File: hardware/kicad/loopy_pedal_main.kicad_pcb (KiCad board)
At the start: 2 copper layers, 82 x 94 mm, 89 parts, among them J1 USB, J10 MOCO, J11 IND, J12 UNDO, J13 MODE, J14 TRACK1, J15 TRACK2, J16 TRACK3, J17 TRACK4, J18 CLEAR, J19 BANK, J2 9V, J3 RECPLAY, J4 STOP, J5 RING, J6 ICSP U1, J7 ICSP U2, J8 MIDI OUT, J9 MIDI IN, Q1 AO3401A, SW1 RST U1, SW2 RST U2, U1 ATmega328P-A, U10 74AHCT1G08, U2 ATmega16U2-A, U3 AP63203WU, U4 74AHCT1G125, U5 LM66100DCK, U6 LM66100DCK, U7 USBLC6-2SC6, U8 74AHCT1G125, U9 H11L1, Y1 16MHz, Y2 16MHz

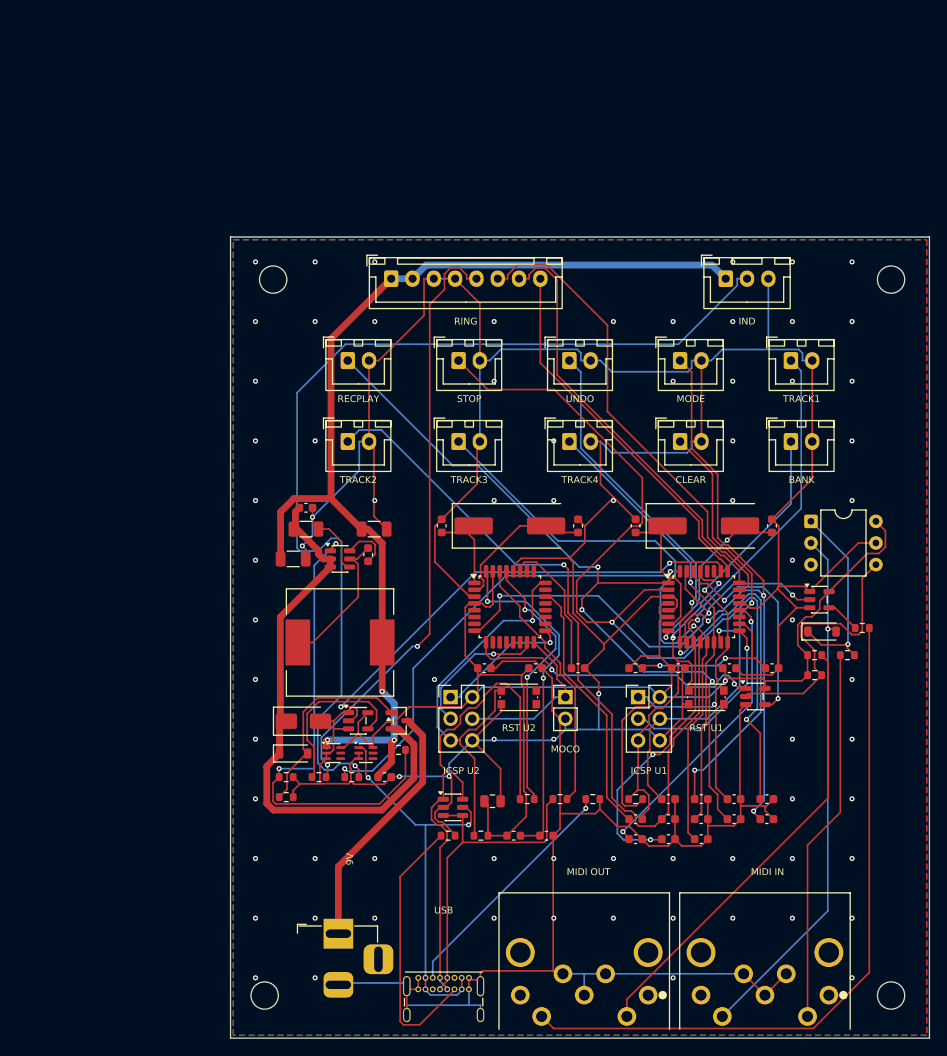
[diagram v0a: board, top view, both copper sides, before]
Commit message: feat(hardware): THT Loopy pedal main + ring boards, fab-ready
Through-hole MIDI looper foot-pedal: two KiCad 10 boards generated from
SKiDL + a scripted place/route pipeline, ready for JLCPCB bare-board fab.

Main board (94x96mm):
- Arduino Pro Micro (ATmega32U4) native USB-MIDI, buffered DIN MIDI OUT
  (74AHCT125), opto-isolated DIN MIDI IN (H11L1)
- 9V centre-negative barrel -> reverse-protection Schottky + TVS -> buck
  (+5V_LED for the LED ring); Pro Micro powered via RAW (onboard reg -> VCC)
- 10 footswitch headers, faceplate RESET (J20) + 6-pin ICSP (J21) recovery
- Fully silk-labelled (functions + component values), 4x M3 GND-bonded holes

Ring board (60mm round):
- Hosts an off-the-shelf 16-LED WS2812 NeoPixel module + EC11 encoder,
  8-pin link to the main board; 4-pad module mount (DIN/+5V/GND + DOUT post)

Both boards DRC-clean; gerbers + BOM/CPL in fab/. Vendored footprints and
3D models in loopy.pretty/. Plan-of-record in loopy_pedal_pcb_tht_plan.md.
Firmware skeleton (USB-MIDI + Serial1 DIN + footswitch debounce) in firmware/.
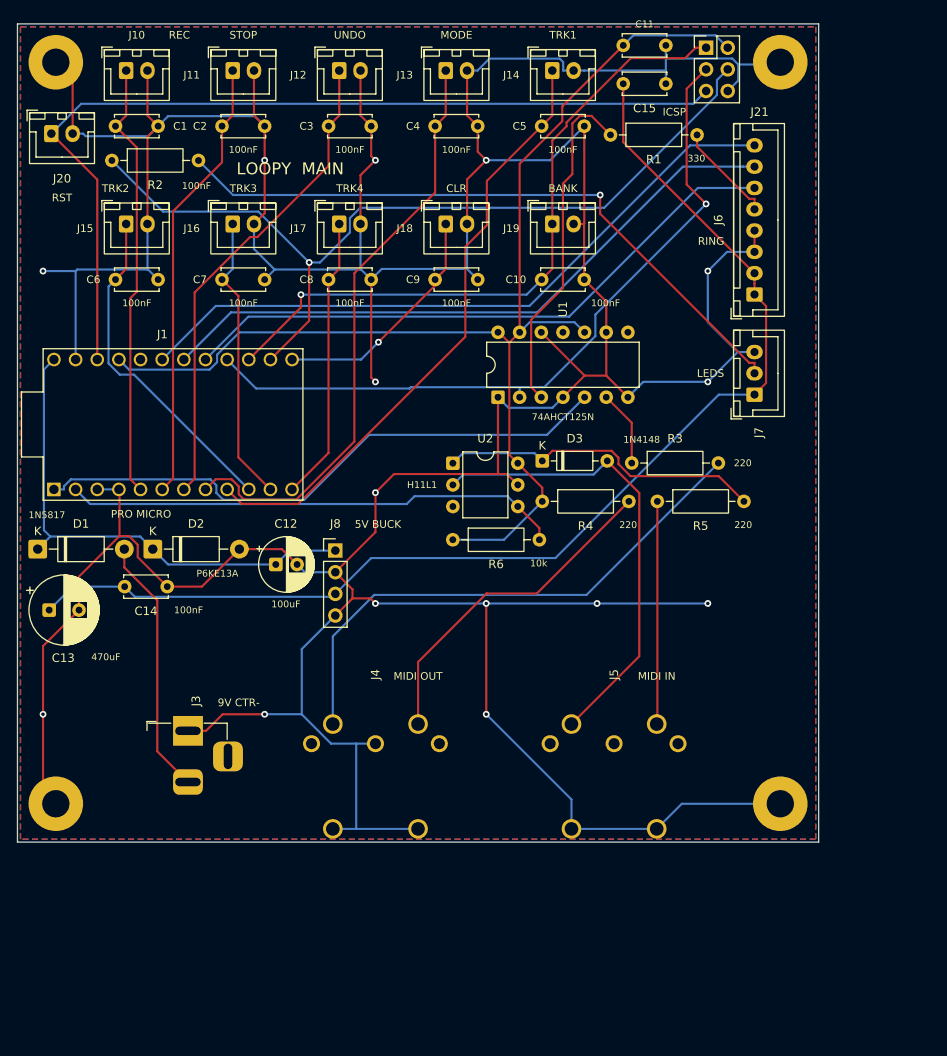
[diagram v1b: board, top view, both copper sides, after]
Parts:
- removed C16, C19, C20, C25, C28, C29, C30: 100nF, C_0603_1608Metric
- removed C17, C18: 1nF, C_0603_1608Metric
- removed C21: 1uF, C_0603_1608Metric
- removed C22, C23: 22pF, C_0603_1608Metric
- removed C24, C26, C27: 22uF, C_1206_3216Metric
- removed FB1, FB2: FerriteBead, L_0603_1608Metric
- removed J2: 9V, BarrelJack_Horizontal
- removed J9: MIDI IN, MIDI_DIN5_RA
- removed L1: 10uH, L_12x12mm_H8mm
- removed Q1: AO3401A, SOT-23
- removed R10, R11, R12: 220, R_0603_1608Metric
- removed R13, R8: 10k, R_0603_1608Metric
- removed R14, R9: 330, R_0603_1608Metric
- removed R15: 100k, R_0603_1608Metric
- removed R7: 52.3k, R_0603_1608Metric
- removed SW1: RST U1, SW_Push_1P1T_NO_CK_KMR2
- removed SW2: RST U2, SW_Push_1P1T_NO_CK_KMR2
- removed U10: 74AHCT1G08, SOT-23-5
- removed U3: AP63203WU, SOT-23-6
- removed U4, U8: 74AHCT1G125, SOT-23-5
- removed U5, U6: LM66100DCK, SOT-363_SC-70-6
- removed U7: USBLC6-2SC6, SOT-23-6
- removed U9: H11L1, DIP-6_W7.62mm
- removed Y1, Y2: 16MHz, Crystal_SMD_HC49-SD
- added J20: RESET, JST_XH_B2B-XH-A_1x02_P2.50mm_Vertical, F.Cu at (8.97, 17.9)
- added J21: ICSP, PinHeader_2x03_P2.54mm_Vertical, F.Cu at (85.8, 7.79)
- C1, C10, C11, C14, C15, C2, C5, C6, C8, C9: footprint C_0603_1608Metric -> C_Disc_D5.0mm_W2.5mm_P5.00mm
- C12: value 100nF -> 100uF; footprint C_0603_1608Metric -> CP_Radial_D6.3mm_P2.50mm
- C13: value 100nF -> 470uF; footprint C_0603_1608Metric -> CP_Radial_D8.0mm_P3.50mm
- C3, C4: value 22pF -> 100nF; footprint C_0603_1608Metric -> C_Disc_D5.0mm_W2.5mm_P5.00mm
- C7: value 10uF -> 100nF; footprint C_0805_2012Metric -> C_Disc_D5.0mm_W2.5mm_P5.00mm
- D1: value SMAJ12A -> 1N5817; footprint D_SMA -> D_DO-41_SOD81_P10.16mm_Horizontal
- D2: value 1N4148 -> P6KE13A; footprint D_SOD-123 -> D_DO-41_SOD81_P10.16mm_Horizontal
- D3: value 10V -> 1N4148; footprint D_SOD-123 -> D_DO-35_SOD27_P7.62mm_Horizontal
- H1, H2, H3, H4: value MountingHole_3.2mm_M3 -> MountingHole_3.2mm_M3_Pad; footprint MountingHole_3.2mm_M3 -> MountingHole_3.2mm_M3_Pad
- J1: value USB -> ProMicro; footprint USB_C_Receptacle_GCT_USB4085 -> ProMicro
- J10: value MOCO -> FSW_RECPLAY; footprint PinHeader_1x02_P2.54mm_Vertical -> JST_XH_B2B-XH-A_1x02_P2.50mm_Vertical
- J11: value IND -> FSW_STOP; footprint JST_XH_B3B-XH-A_1x03_P2.50mm_Vertical -> JST_XH_B2B-XH-A_1x02_P2.50mm_Vertical
- J12: value UNDO -> FSW_UNDO
- J13: value MODE -> FSW_MODE
- J14: value TRACK1 -> FSW_TRACK1
- J15: value TRACK2 -> FSW_TRACK2
- J16: value TRACK3 -> FSW_TRACK3
- J17: value TRACK4 -> FSW_TRACK4
- J18: value CLEAR -> FSW_CLEAR
- J19: value BANK -> FSW_BANK
- J3: value RECPLAY -> Barrel_Jack; footprint JST_XH_B2B-XH-A_1x02_P2.50mm_Vertical -> BarrelJack_Horizontal
- J4: value STOP -> MIDI_DIN5_RA; footprint JST_XH_B2B-XH-A_1x02_P2.50mm_Vertical -> MIDI_DIN5_RA
- J5: value RING -> MIDI_DIN5_RA; footprint JST_XH_B8B-XH-A_1x08_P2.50mm_Vertical -> MIDI_DIN5_RA
- J6: value ICSP U1 -> Conn_01x08; footprint PinHeader_2x03_P2.54mm_Vertical -> JST_XH_B8B-XH-A_1x08_P2.50mm_Vertical
- J7: value ICSP U2 -> Conn_01x03; footprint PinHeader_2x03_P2.54mm_Vertical -> JST_XH_B3B-XH-A_1x03_P2.50mm_Vertical
- J8: value MIDI OUT -> BUCK_5V; footprint MIDI_DIN5_RA -> PinHeader_1x04_P2.54mm_Vertical
- R1: value 10k -> 330; footprint R_0603_1608Metric -> R_Axial_DIN0207_L6.3mm_D2.5mm_P10.16mm_Horizontal
- R2: value 22 -> 330; footprint R_0603_1608Metric -> R_Axial_DIN0207_L6.3mm_D2.5mm_P10.16mm_Horizontal
- R3: value 22 -> 220; footprint R_0603_1608Metric -> R_Axial_DIN0207_L6.3mm_D2.5mm_P10.16mm_Horizontal
- R4: value 10k -> 220; footprint R_0603_1608Metric -> R_Axial_DIN0207_L6.3mm_D2.5mm_P10.16mm_Horizontal
- R5: value 5.1k -> 220; footprint R_0603_1608Metric -> R_Axial_DIN0207_L6.3mm_D2.5mm_P10.16mm_Horizontal
- R6: value 5.1k -> 10k; footprint R_0603_1608Metric -> R_Axial_DIN0207_L6.3mm_D2.5mm_P10.16mm_Horizontal
- U1: value ATmega328P-A -> 74AHCT125N; footprint TQFP-32_7x7mm_P0.8mm -> DIP-14_W7.62mm
- U2: value ATmega16U2-A -> H11L1; footprint TQFP-32_7x7mm_P0.8mm -> DIP-6_W7.62mm
- moved C1 99.9 mm to (16.5, 17.0)
- moved C2 96.7 mm to (29.0, 17.0)
- moved J10 89.8 mm to (17.8, 10.5)
- moved R2 89.4 mm to (16.1, 21.0)
- moved C15 89.1 mm to (76.1, 12.0)
- moved C11 88.9 mm to (76.1, 7.53)
- moved C6 85.2 mm to (16.5, 35.0)
- moved D2 79.1 mm to (20.9, 66.6)
- moved R1 78.0 mm to (74.6, 18.0)
- moved C13 77.5 mm to (8.72, 73.8)
- moved C8 72.8 mm to (41.5, 35.0)
- moved C9 72.4 mm to (54.0, 35.0)
- moved J1 71.0 mm to (23.2, 52.0)
- moved C14 69.4 mm to (17.6, 71.0)
- moved C7 68.9 mm to (29.0, 35.0)
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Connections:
- C1 pad 1: N$1 -> SW_RECPLAY
- C10 pad 1: SW_STOP -> SW_BANK
- C11 pad 1: SW_UNDO -> +5V
- C12 pad 1: SW_MODE -> +9V
- C13 pad 1: SW_TRACK1 -> +5V_LED
- C14 pad 1: SW_TRACK2 -> +5V_LED
- C15 pad 1: SW_TRACK3 -> +5V_LED
- C2 pad 1: N$2 -> SW_STOP
- C3 pad 1: N$3 -> SW_UNDO
- C4 pad 1: N$4 -> SW_MODE
- C5 pad 1: +5V -> SW_TRACK1
- C6 pad 1: +5V -> SW_TRACK2
- C7 pad 1: +5V -> SW_TRACK3
- C8 pad 1: DTR -> SW_TRACK4
- C8 pad 2: RST_328 -> GND
- C9 pad 1: SW_RECPLAY -> SW_CLEAR
- D1 pad 2: GND -> VIN_RAW
- D2 pad 1: N$20 -> +9V
- D2 pad 2: N$21 -> GND
- D3 pad 1: +9V -> N$4
- D3 pad 2: Q1_GATE -> N$5
- J10 pad 1: N$11 -> SW_RECPLAY
- J11 pad 1: +5V_LED -> SW_STOP
- J11 pad 2: IND_DATA_OUT -> GND
- J3 pad 1: SW_RECPLAY -> GND
- J3 pad 2: GND -> VIN_RAW
- J4 pad 1: SW_STOP -> (no net)
- J5 pad 1: +5V_LED -> (no net)
- J5 pad 2: +5V_LED -> (no net)
- J5 pad 3: GND -> (no net)
- J5 pad 4: GND -> N$3
- J5 pad 5: RING_DATA_OUT -> N$5
- J5 pad 6: ENC_A -> GND
- J5 pad 7: ENC_B -> GND
- J6 pad 1: SW_BANK -> +5V_LED
- J6 pad 2: +5V -> +5V_LED
- J6 pad 3: N$5 -> GND
- J6 pad 4: SW_CLEAR -> GND
- J6 pad 5: RST_328 -> RING_DATA_OUT
- J6 pad 6: GND -> ENC_A
- J7 pad 1: N$12 -> +5V_LED
- J7 pad 2: +5V -> IND_DATA_OUT
- J7 pad 3: N$13 -> GND
- J8 pad 1: (no net) -> +9V
- J8 pad 3: (no net) -> +5V_LED
- J8 pad 4: N$18 -> GND
- R1 pad 1: RST_328 -> RING_DATA_BUF
- R1 pad 2: +5V -> RING_DATA_OUT
- R2 pad 1: USB_D+ -> IND_DATA
- R2 pad 2: N$9 -> IND_DATA_OUT
- R3 pad 1: USB_D- -> MIDI_OUT_BUF
- R3 pad 2: N$10 -> N$1
- R4 pad 1: RST_16 -> +5V
- R4 pad 2: +5V -> N$2
- R5 pad 1: N$14 -> N$3
- R5 pad 2: GND -> N$4
- R6 pad 1: N$15 -> +5V
- R6 pad 2: GND -> UART_RX
- U1 pad 1: SW_RECPLAY -> GND
- U1 pad 10: SW_MODE -> +5V
- U1 pad 11: SW_TRACK1 -> (no net)
- U1 pad 12: SW_TRACK2 -> GND
- U1 pad 13: SW_TRACK3 -> +5V
- U1 pad 14: SW_TRACK4 -> +5V
- U1 pad 2: SW_STOP -> RING_DATA
- U1 pad 3: GND -> RING_DATA_BUF
- U1 pad 4: +5V -> GND
- U1 pad 5: GND -> UART_TX
- U1 pad 6: +5V -> MIDI_OUT_BUF
- U1 pad 7: N$3 -> GND
- U1 pad 8: N$4 -> (no net)
- U1 pad 9: SW_UNDO -> GND
- U2 pad 1: N$7 -> N$4
- U2 pad 2: N$8 -> N$5
- U2 pad 3: GND -> (no net)
- U2 pad 4: +5V -> UART_RX
- U2 pad 5: (no net) -> GND
- U2 pad 6: (no net) -> +5V
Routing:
- net RST: track 0.00 -> 107.6 mm
- net N$17: track 82.2 -> 0.00 mm
- net N$21: track 62.6 -> 0.00 mm, vias 1 -> 0
- net USB_D+: track 62.4 -> 0.00 mm
- net RING_DATA_OUT: track 70.6 -> 11.9 mm, vias 2 -> 0
- net FB: track 57.0 -> 0.00 mm, vias 2 -> 0
- net SW_STOP: track 105.8 -> 52.6 mm, vias 2 -> 0
- net SW_TRACK2: track 92.9 -> 39.8 mm, vias 1 -> 0
- net N$18: track 52.5 -> 0.00 mm
- net RST_16: track 48.5 -> 0.00 mm, vias 1 -> 0
- net IND_DATA: track 54.4 -> 101.9 mm, vias 2 -> 1
- net VBUS: track 46.7 -> 0.00 mm, vias 2 -> 0
- net N$19: track 44.0 -> 0.00 mm
- net RST_328: track 43.6 -> 0.00 mm, vias 2 -> 0
- net N$1: track 20.4 -> 64.0 mm, vias 2 -> 0
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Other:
- board size 82 x 94 mm -> 94 x 96 mm
- board text added: "100nF"
- board text added: "100uF"
- board text added: "10k"
- board text added: "1N4148"
- board text added: "1N5817"
- board text added: "220"
- board text added: "330"
- board text added: "470uF"
- board text added: "5V BUCK"
- board text added: "74AHCT125N"
- board text added: "9V CTR-"
- board text added: "BANK"
- board text added: "CLR"
- board text added: "H11L1"
- board text added: "ICSP"
- board text added: "LEDS"
- board text added: "LOOPY MAIN"
- board text added: "MIDI IN"
- board text added: "MIDI OUT"
- board text added: "MODE"
- board text added: "P6KE13A"
- board text added: "PRO MICRO"
- board text added: "REC"
- board text added: "RING"
- board text added: "RST"
- board text added: "STOP"
- board text added: "TRK1"
- board text added: "TRK2"
- board text added: "TRK3"
- board text added: "TRK4"
- board text added: "UNDO"

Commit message: feat(hardware): main-board respin — on-board buck, floorplan, wide rails + ground planes
Reworked the loopy_pedal main board:
- MP1584 buck mounts flat on its own footprint (loopy:BuckModule_MP1584 + STEP),
  no longer a 1x4 header; fixed the SW_TRACK4<->R7/R8 short by relocating the
  A3-sense divider; added local decoupling C11/C16 for U1/U2.
- Floorplan: power grouped in the bottom band, MIDI on the right, Pro Micro on
  the left (USB accessible); force-directed placement + Freerouting.
- Power nets 0.8mm / +5V 0.5mm net classes, dual F.Cu+B.Cu ground planes.
- Ring board: component values onto the silkscreen.
DRC: main + ring both 0 violations, 0 unconnected.
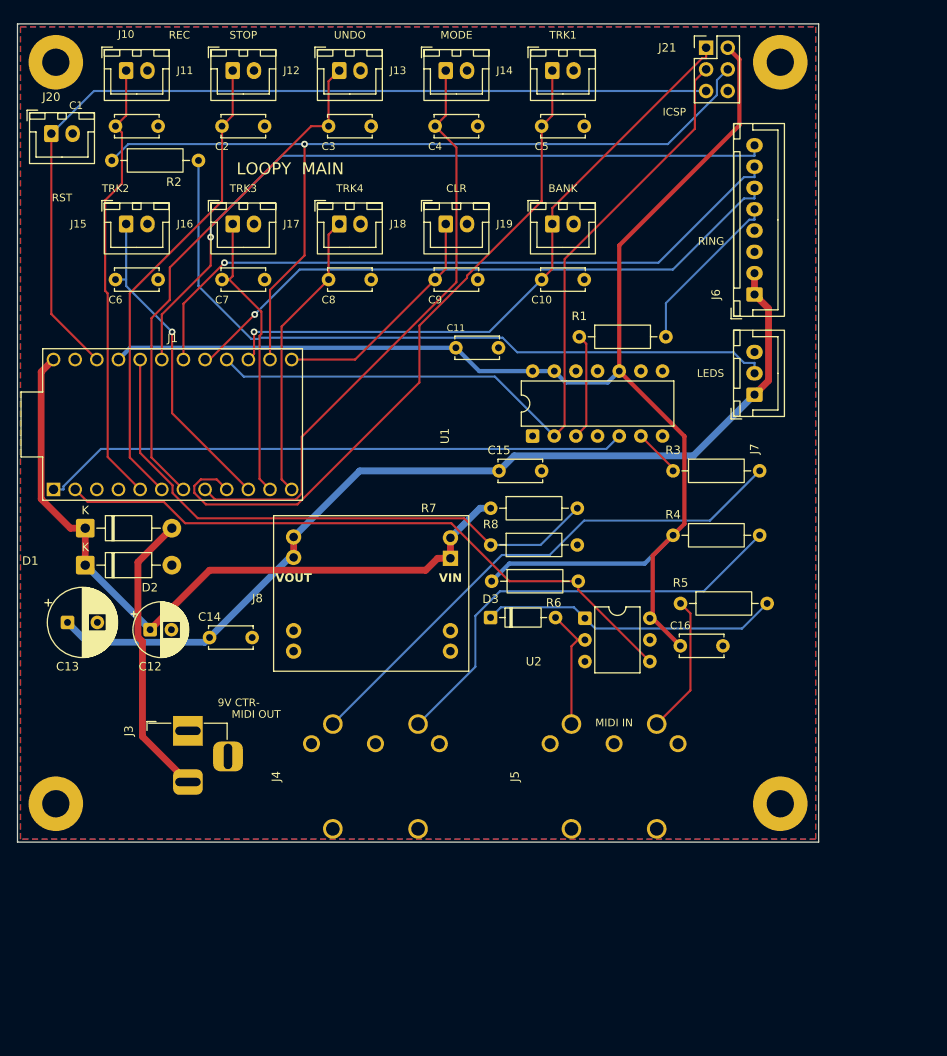
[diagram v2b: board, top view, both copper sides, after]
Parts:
- added C16: 100nF, C_Disc_D5.0mm_W2.5mm_P5.00mm, F.Cu at (82.8, 78.0)
- added R7: 100k, R_Axial_DIN0207_L6.3mm_D2.5mm_P10.16mm_Horizontal, F.Cu at (60.5, 61.8)
- added R8: 47k, R_Axial_DIN0207_L6.3mm_D2.5mm_P10.16mm_Horizontal, F.Cu at (60.5, 66.1)
- J8: value BUCK_5V -> MP1584; footprint PinHeader_1x04_P2.54mm_Vertical -> BuckModule_MP1584
- moved C15 47.7 mm to (61.5, 57.4)
- moved C11 40.5 mm to (56.4, 43.0)
- moved R1 24.0 mm to (70.9, 41.7)
- moved U2 23.9 mm to (71.6, 74.7)
- moved D3 19.4 mm to (60.5, 74.7)
- moved C12 16.6 mm to (20.6, 76.1)
- moved R4 15.9 mm to (81.9, 65.0)
- moved R5 12.3 mm to (82.8, 73.0)
- moved C14 11.6 mm to (27.5, 77.0)
- moved D2 8.14 mm to (13.0, 68.5)
- moved J8 6.72 mm to (46.0, 72.4), turned to 180 degrees
- moved R6 6.67 mm to (60.6, 70.4)
- moved U1 6.10 mm to (65.4, 53.4)
- moved D1 6.10 mm to (13.0, 64.2)
- moved R3 4.93 mm to (81.9, 57.4)
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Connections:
- J1 pad 20: (no net) -> LED_PWR_SENSE
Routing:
- net GND: track 627.1 -> 0.00 mm, vias 15 -> 0
- net LED_PWR_SENSE: track 0.00 -> 69.0 mm
- net N$5: track 55.0 -> 14.7 mm
- net RING_DATA_BUF: track 40.4 -> 12.5 mm
- net +5V_LED: track 138.2 -> 110.6 mm
- net +9V: track 59.1 -> 85.9 mm
- net +5V: track 144.1 -> 168.1 mm
- net UART_RX: track 58.4 -> 76.4 mm
- net N$2: track 39.8 -> 52.8 mm
- net N$3: track 26.2 -> 16.3 mm
- net SW_TRACK1: track 72.2 -> 81.4 mm
- net RING_DATA_OUT: track 11.9 -> 19.6 mm
- net IND_DATA_OUT: track 77.6 -> 85.0 mm, vias 1 -> 0
- net ENC_SW: track 79.9 -> 86.4 mm, vias 0 -> 1
- net RING_DATA: track 86.9 -> 92.6 mm, vias 1 -> 0
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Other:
- board text removed: "100nF"
- board text removed: "100uF"
- board text removed: "10k"
- board text removed: "1N4148"
- board text removed: "1N5817"
- board text removed: "220"
- board text removed: "330"
- board text removed: "470uF"
- board text removed: "5V BUCK"
- board text removed: "74AHCT125N"
- board text removed: "H11L1"
- board text removed: "P6KE13A"
- board text removed: "PRO MICRO"
